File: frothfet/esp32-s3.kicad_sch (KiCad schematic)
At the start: 47 parts, among them J1 USB_TYPE_C_16PIN, Q20 FDC6330L, Q21 S8050, Q22 S8050, SW1 RESET, SW2 BOOT, U1 ESP32-S3-WROOM-1-N16R8, U33 USBLC6-2SC6, U34 XC6210B332MR, U35 CH334F, U36 CH343P, Y1 12Mhz, Y2 32.768kHz

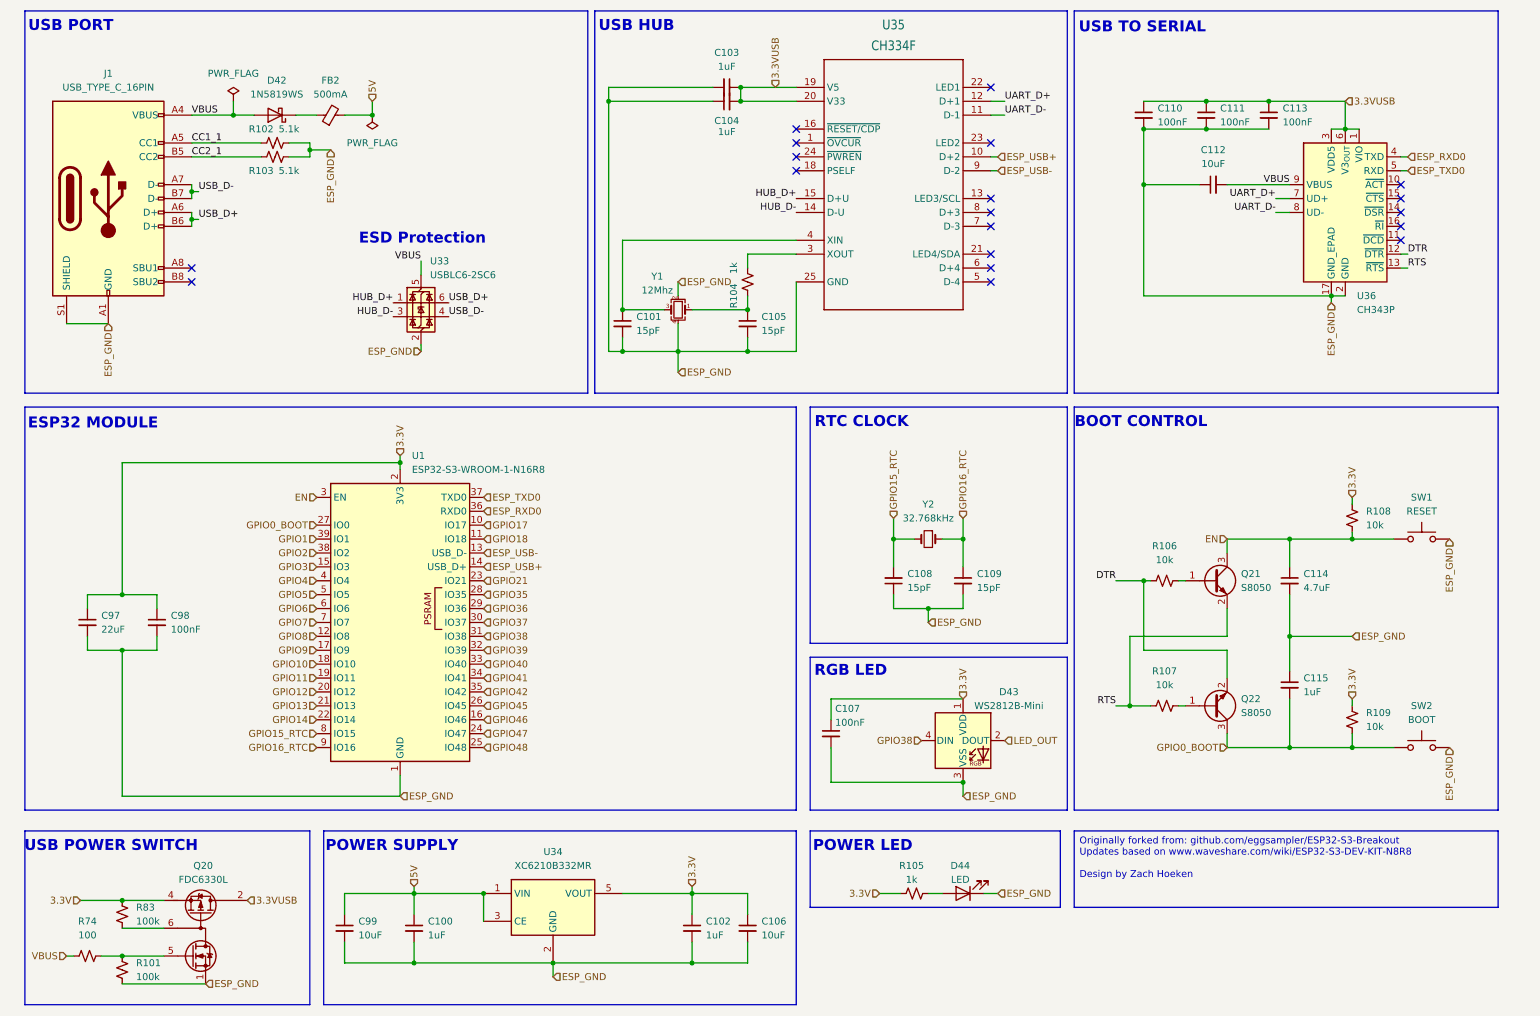
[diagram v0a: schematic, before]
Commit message: updated calculations, updated esp32-s3 schematic, updated layout.
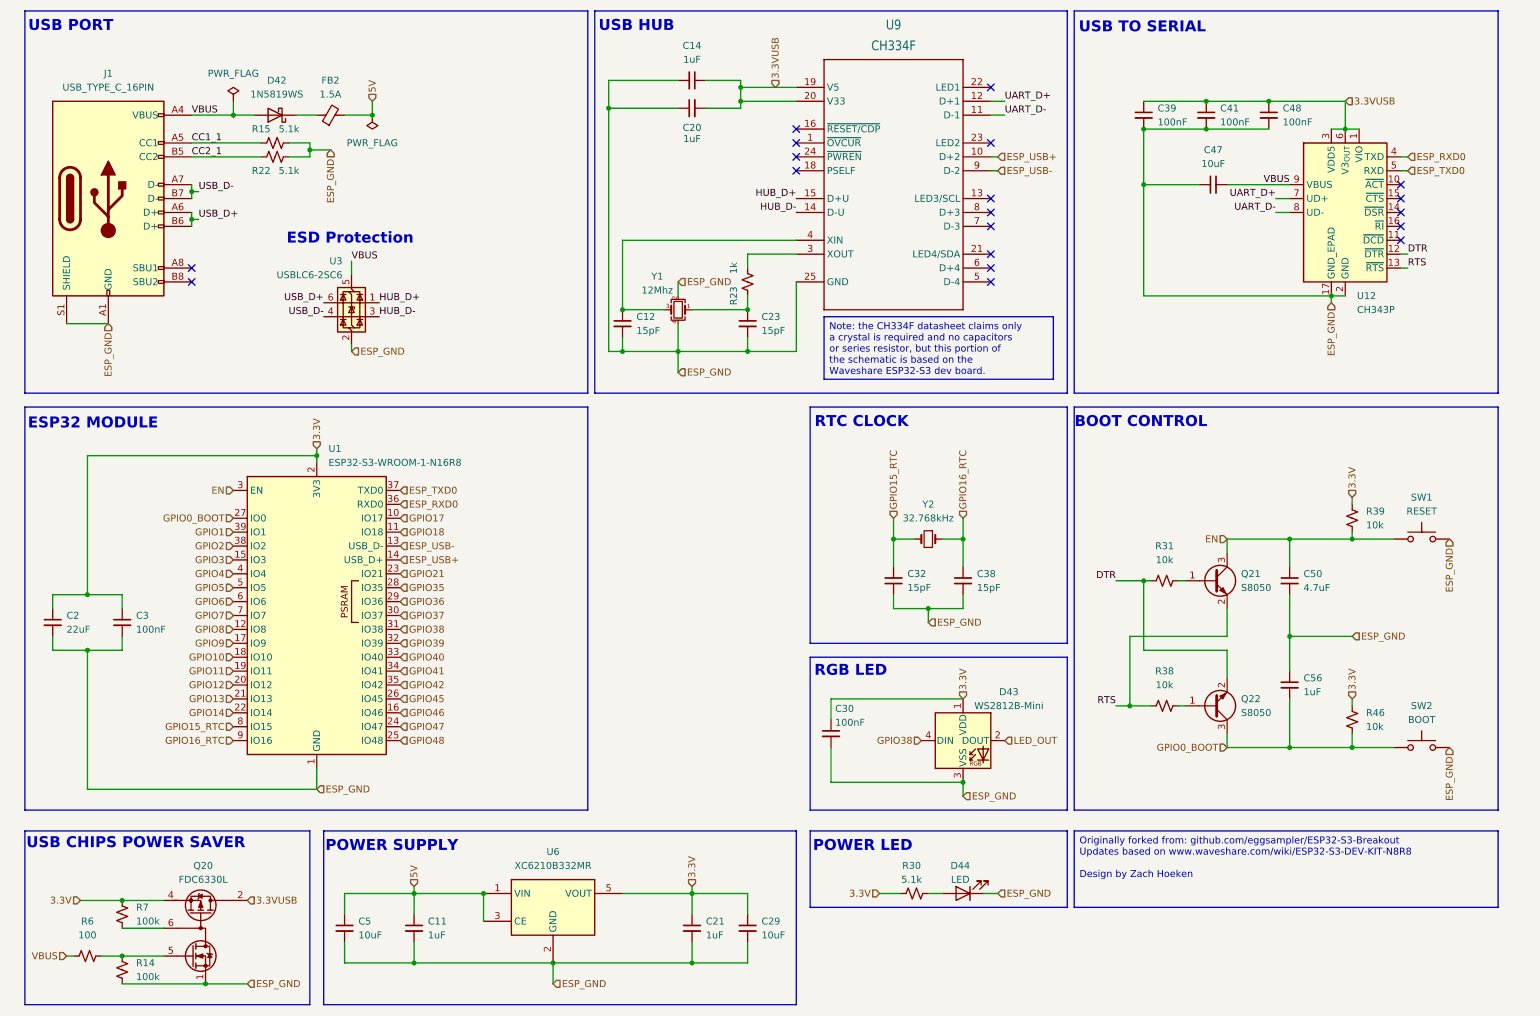
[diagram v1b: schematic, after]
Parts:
- FB2: value 500mA -> 1.5A; footprint Fuse:Fuse_0603_1608Metric -> Fuse:Fuse_1206_3216Metric; LCSC C69679 -> C2760275
- R15: renamed from R102; LCSC C105580 -> (none)
- R22: renamed from R103; LCSC C105580 -> (none)
- R30: renamed from R105; value 1k -> 5.1k
- renumbered C100 to C11, C101 to C12, C103 to C14, C97 to C2, C104 to C20, C102 to C21, C105 to C23, C106 to C29, C98 to C3, C107 to C30, C108 to C32, C109 to C38, C110 to C39, C111 to C41, C112 to C47, C113 to C48, C99 to C5, C114 to C50, C115 to C56, R101 to R14, R104 to R23, R106 to R31, R107 to R38, R108 to R39, R109 to R46, R74 to R6, R83 to R7, U36 to U12, U33 to U3, U34 to U6, U35 to U9
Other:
- note added: "USB CHIPS POWER SAVER"
- note removed: "USB POWER SWITCH"
- title: (none) -> https://github.com/hoeken/ESP32-S3-Template
- moved on the sheet: C14, C2, C20, C3, U1, U3

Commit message: worked on the bom and footprint placement
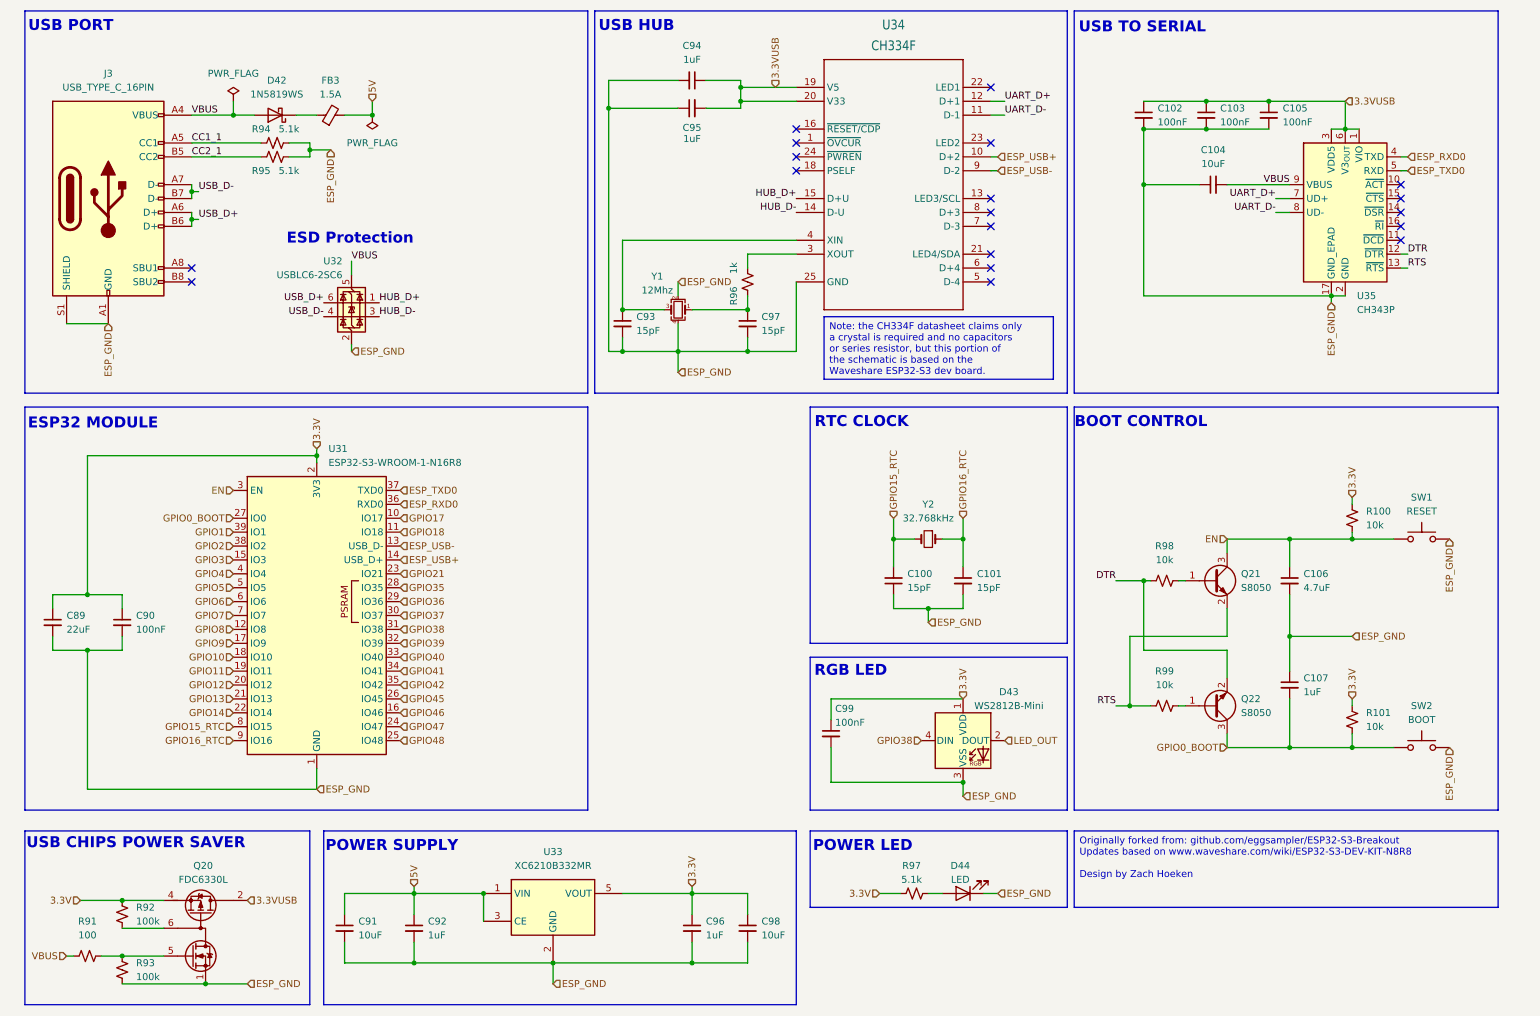
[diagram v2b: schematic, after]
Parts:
- D44: LCSC (none) -> C2286
- renumbered C32 to C100, C38 to C101, C39 to C102, C41 to C103, C47 to C104, C48 to C105, C50 to C106, C56 to C107, C2 to C89, C3 to C90, C5 to C91, C11 to C92, C12 to C93, C14 to C94, C20 to C95, C21 to C96, C23 to C97, C29 to C98, C30 to C99, FB2 to FB3, J1 to J3, R39 to R100, R46 to R101, R6 to R91, R7 to R92, R14 to R93, R15 to R94, R22 to R95, R23 to R96, R30 to R97, R31 to R98, R38 to R99, U1 to U31, U3 to U32, U6 to U33, U9 to U34, U12 to U35

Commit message: lots of work on the analog system
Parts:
- SW1, SW2: footprint Button_Switch_SMD:SW_SPST_B3U-1000P -> Button_Switch_THT:SW_Tactile_SPST_Angled_PTS645Vx58-2LFS
- renumbered C94 to C100, C95 to C101, C96 to C102, C97 to C103, C98 to C104, C99 to C105, C100 to C106, C101 to C107, C102 to C108, C103 to C109, C104 to C110, C105 to C111, C106 to C112, C107 to C113, C89 to C95, C90 to C96, C91 to C97, C92 to C98, C93 to C99, FB3 to FB2
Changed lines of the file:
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@@
 		(dnp no)
 		(fields_autoplaced yes)
-		(property "Reference" "#FLG012"
+		(property "Reference" "#FLG011"
 			(at 77.47 34.925 0)
 			(effects
@@
 			(project "frothfet"
 				(path "/c83c6236-96e9-46ad-9d7a-9e2efa4a7966/777fe0ac-daa5-4cfe-9bd1-5eba0a425019"
-					(reference "#FLG012")
+					(reference "#FLG011")
 					(unit 1)
 				)
@@
 		(dnp no)
 		(fields_autoplaced yes)
-		(property "Reference" "C92"
+		(property "Reference" "C98"
 			(at 87.63 180.3462 0)
 			(effects
@@
 			(project "frothfet"
 				(path "/c83c6236-96e9-46ad-9d7a-9e2efa4a7966/777fe0ac-daa5-4cfe-9bd1-5eba0a425019"
-					(reference "C92")
+					(reference "C98")
 					(unit 1)
 				)
@@
 		(dnp no)
 		(fields_autoplaced yes)
-		(property "Reference" "C89"
+		(property "Reference" "C95"
 			(at 21.59 124.4662 0)
 			(effects
@@
 			(project "frothfet"
 				(path "/c83c6236-96e9-46ad-9d7a-9e2efa4a7966/777fe0ac-daa5-4cfe-9bd1-5eba0a425019"
-					(reference "C89")
+					(reference "C95")
 					(unit 1)
 				)
@@
 		(dnp no)
 		(fields_autoplaced yes)
-		(property "Reference" "C101"
+		(property "Reference" "C107"
 			(at 187.96 116.8462 0)
 			(effects
@@
 			(project "frothfet"
 				(path "/c83c6236-96e9-46ad-9d7a-9e2efa4a7966/777fe0ac-daa5-4cfe-9bd1-5eba0a425019"
-					(reference "C101")
+					(reference "C107")
 					(unit 1)
 				)
@@
 		(on_board yes)
 		(dnp no)
-		(property "Reference" "C97"
+		(property "Reference" "C103"
 			(at 148.59 69.8562 0)
 			(effects
@@
 			(project "frothfet"
 				(path "/c83c6236-96e9-46ad-9d7a-9e2efa4a7966/777fe0ac-daa5-4cfe-9bd1-5eba0a425019"
-					(reference "C97")
+					(reference "C103")
 					(unit 1)
 				)
@@
 		(dnp no)
 		(fields_autoplaced yes)
-		(property "Reference" "C103"
+		(property "Reference" "C109"
 			(at 232.41 31.7562 0)
 			(effects
@@
 			(project "frothfet"
 				(path "/c83c6236-96e9-46ad-9d7a-9e2efa4a7966/777fe0ac-daa5-4cfe-9bd1-5eba0a425019"
-					(reference "C103")
+					(reference "C109")
 					(unit 1)
 				)
@@
 		(dnp no)
 		(fields_autoplaced yes)
-		(property "Reference" "C106"
+		(property "Reference" "C112"
 			(at 247.65 116.8462 0)
 			(effects
@@
 			(project "frothfet"
 				(path "/c83c6236-96e9-46ad-9d7a-9e2efa4a7966/777fe0ac-daa5-4cfe-9bd1-5eba0a425019"
-					(reference "C106")
+					(reference "C112")
 					(unit 1)
 				)
@@
 		(on_board yes)
 		(dnp no)
-		(property "Reference" "C94"
+		(property "Reference" "C100"
 			(at 135.8836 20.32 90)
 			(effects
@@
 			(project "frothfet"
 				(path "/c83c6236-96e9-46ad-9d7a-9e2efa4a7966/777fe0ac-daa5-4cfe-9bd1-5eba0a425019"
-					(reference "C94")
+					(reference "C100")
 					(unit 1)
 				)
@@
 		(dnp no)
 		(fields_autoplaced yes)
-		(property "Reference" "C107"
+		(property "Reference" "C113"
 			(at 247.65 135.8962 0)
 			(effects
@@
 			(project "frothfet"
 				(path "/c83c6236-96e9-46ad-9d7a-9e2efa4a7966/777fe0ac-daa5-4cfe-9bd1-5eba0a425019"
-					(reference "C107")
+					(reference "C113")
 					(unit 1)
 				)
@@
 		(on_board yes)
 		(dnp no)
-		(property "Reference" "C95"
+		(property "Reference" "C101"
 			(at 135.89 35.306 90)
 			(effects
@@
 			(project "frothfet"
 				(path "/c83c6236-96e9-46ad-9d7a-9e2efa4a7966/777fe0ac-daa5-4cfe-9bd1-5eba0a425019"
-					(reference "C95")
+					(reference "C101")
 					(unit 1)
 				)
@@
 		(dnp no)
 		(fields_autoplaced yes)
-		(property "Reference" "C90"
+		(property "Reference" "C96"
 			(at 34.29 124.4662 0)
 			(effects
@@
 			(project "frothfet"
 				(path "/c83c6236-96e9-46ad-9d7a-9e2efa4a7966/777fe0ac-daa5-4cfe-9bd1-5eba0a425019"
-					(reference "C90")
+					(reference "C96")
 					(unit 1)
 				)
@@
 			)
 		)
-		(property "Footprint" "Button_Switch_SMD:SW_SPST_B3U-1000P"
+		(property "Footprint" "Button_Switch_THT:SW_Tactile_SPST_Angled_PTS645Vx58-2LFS"
 			(at 269.24 105.41 0)
 			(effects
@@
 		(on_board yes)
 		(dnp no)
-		(property "Reference" "C102"
+		(property "Reference" "C108"
 			(at 220.98 31.7562 0)
 			(effects
@@
 			(project "frothfet"
 				(path "/c83c6236-96e9-46ad-9d7a-9e2efa4a7966/777fe0ac-daa5-4cfe-9bd1-5eba0a425019"
-					(reference "C102")
+					(reference "C108")
 					(unit 1)
 				)
@@
 		(dnp no)
 		(fields_autoplaced yes)
-		(property "Reference" "C93"
+		(property "Reference" "C99"
 			(at 125.73 69.8562 0)
 			(effects
@@
 			(project "frothfet"
 				(path "/c83c6236-96e9-46ad-9d7a-9e2efa4a7966/777fe0ac-daa5-4cfe-9bd1-5eba0a425019"
-					(reference "C93")
+					(reference "C99")
 					(unit 1)
 				)
@@
 		(dnp no)
 		(fields_autoplaced yes)
-		(property "Reference" "C91"
+		(property "Reference" "C97"
 			(at 74.93 180.3462 0)
 			(effects
@@
 			(project "frothfet"
 				(path "/c83c6236-96e9-46ad-9d7a-9e2efa4a7966/777fe0ac-daa5-4cfe-9bd1-5eba0a425019"
-					(reference "C91")
+					(reference "C97")
 					(unit 1)
 				)
@@
 			)
 		)
-		(property "Footprint" "Button_Switch_SMD:SW_SPST_B3U-1000P"
+		(property "Footprint" "Button_Switch_THT:SW_Tactile_SPST_Angled_PTS645Vx58-2LFS"
 			(at 269.24 143.51 0)
 			(effects
@@
 		(dnp no)
 		(fields_autoplaced yes)
-		(property "Reference" "C105"
+		(property "Reference" "C111"
 			(at 243.84 31.7562 0)
 			(effects
@@
 			(project "frothfet"
 				(path "/c83c6236-96e9-46ad-9d7a-9e2efa4a7966/777fe0ac-daa5-4cfe-9bd1-5eba0a425019"
-					(reference "C105")
+					(reference "C111")
 					(unit 1)
 				)
@@
 		(dnp no)
 		(fields_autoplaced yes)
-		(property "Reference" "FB3"
+		(property "Reference" "FB2"
 			(at 69.8119 26.67 90)
 			(effects
@@
 			(project "frothfet"
 				(path "/c83c6236-96e9-46ad-9d7a-9e2efa4a7966/777fe0ac-daa5-4cfe-9bd1-5eba0a425019"
-					(reference "FB3")
+					(reference "FB2")
 					(unit 1)
 				)
@@
 		(dnp no)
 		(fields_autoplaced yes)
-		(property "Reference" "C98"
+		(property "Reference" "C104"
 			(at 148.59 180.3462 0)
 			(effects
@@
 			(project "frothfet"
 				(path "/c83c6236-96e9-46ad-9d7a-9e2efa4a7966/777fe0ac-daa5-4cfe-9bd1-5eba0a425019"
-					(reference "C98")
+					(reference "C104")
 					(unit 1)
 				)
@@
 		(on_board yes)
 		(dnp no)
-		(property "Reference" "C99"
+		(property "Reference" "C105"
 			(at 162.052 141.478 0)
 			(effects
@@
 			(project "frothfet"
 				(path "/c83c6236-96e9-46ad-9d7a-9e2efa4a7966/777fe0ac-daa5-4cfe-9bd1-5eba0a425019"
-					(reference "C99")
+					(reference "C105")
 					(unit 1)
 				)
@@
 		(dnp no)
 		(fields_autoplaced yes)
-		(property "Reference" "#FLG011"
+		(property "Reference" "#FLG010"
 			(at 52.07 28.575 0)
 			(effects
@@
 			(project "frothfet"
 				(path "/c83c6236-96e9-46ad-9d7a-9e2efa4a7966/777fe0ac-daa5-4cfe-9bd1-5eba0a425019"
-					(reference "#FLG011")
+					(reference "#FLG010")
 					(unit 1)
 				)
@@
 		(dnp no)
 		(fields_autoplaced yes)
-		(property "Reference" "C104"
+		(property "Reference" "C110"
 			(at 231.1463 39.37 90)
 			(effects
@@
 			(project "frothfet"
 				(path "/c83c6236-96e9-46ad-9d7a-9e2efa4a7966/777fe0ac-daa5-4cfe-9bd1-5eba0a425019"
-					(reference "C104")
+					(reference "C110")
 					(unit 1)
 				)
@@
 		(dnp no)
 		(fields_autoplaced yes)
-		(property "Reference" "C96"
+		(property "Reference" "C102"
 			(at 138.43 180.3462 0)
 			(effects
@@
 			(project "frothfet"
 				(path "/c83c6236-96e9-46ad-9d7a-9e2efa4a7966/777fe0ac-daa5-4cfe-9bd1-5eba0a425019"
-					(reference "C96")
+					(reference "C102")
 					(unit 1)
 				)
@@
 		(dnp no)
 		(fields_autoplaced yes)
-		(property "Reference" "C100"
+		(property "Reference" "C106"
 			(at 175.26 116.8335 0)
 			(effects
@@
 			(project "frothfet"
 				(path "/c83c6236-96e9-46ad-9d7a-9e2efa4a7966/777fe0ac-daa5-4cfe-9bd1-5eba0a425019"
-					(reference "C100")
+					(reference "C106")
 					(unit 1)
 				)
